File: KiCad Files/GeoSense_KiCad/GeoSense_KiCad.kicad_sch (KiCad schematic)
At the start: 127 parts, among them J0 Conn_01x04_Pin, J1 Conn_01x04_Pin, J10 Conn_01x01_Socket, J11 Conn_01x01_Socket, J12 Conn_01x01_Socket, J13 Conn_01x01_Socket, J15 Conn_01x02_Pin, J2 Conn_01x04_Pin, J3 Conn_01x04_Pin, J4 Conn_01x04_Pin, J5 Conn_01x04_Pin, J6 Conn_01x04_Pin, J7 Conn_01x04_Pin, J8 Conn_01x04_Pin, J9 Conn_01x08_Pin, U1 LM324, U1.1 LM334Z, U1.2 LM334Z, U2 LM324, U2.1 LM334Z, U2.2 LM334Z, U3 LM324, U3.1 LM334Z, U3.2 LM334Z, U4 LM324, U4.1 LM334Z, U4.2 LM334Z, U5 LM324, U5.1 LM334Z, U5.2 LM334Z, U6 LM324, U6.1 LM334Z, U6.2 LM334Z, U7 LM324, U7.1 LM334Z, U7.2 LM334Z, U8 LM324, U8.1 LM334Z, U8.2 LM334Z

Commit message: added caps
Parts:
- added C1, C10, C11, C12, C13, C14, C15, C16, C2, C3, C4, C5, C6, C7, C8, C9: C_Small, Capacitor_SMD:C_0603_1608Metric_Pad1.08x0.95mm_HandSolder, symbol Device:C_Small
- U1, U2, U3, U4, U5, U6, U7, U8: footprint (none) -> Package_SO:TSSOP-14_4.4x5mm_P0.65mm
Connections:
- net GND: now also C1.1, C10.2, C11.1, C12.2, C13.1, C14.2, C15.1, C16.2, C2.2, C3.1, C4.2, C5.1, C6.2, C7.1, C8.2, C9.1
- net T1.2 In: now also C2.1
- net T1.C: now also C1.2
- net T2.2 In: now also C4.1
- net T2.C: now also C3.2
- net T3.2 In: now also C6.1
- net T3.C: now also C5.2
- net T4.2 In: now also C8.1
- net T4.C: now also C7.2
- net T5.2 In: now also C10.1
- net T5.C: now also C9.2
- net T6.2 In: now also C12.1
- net T6.C: now also C11.2
- net T7.2 In: now also C14.1
- net T7.C: now also C13.2
- net T8.2 In: now also C16.1
- net T8.C: now also C15.2

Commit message: part way through the pcb design
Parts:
- removed J9: Conn_01x08_Pin, Connector_PinHeader_2.54mm:PinHeader_1x08_P2.54mm_Horizontal, symbol Connector:Conn_01x08_Pin
- added J14, J9: Conn_01x04_Pin, Connector_PinHeader_2.54mm:PinHeader_1x04_P2.54mm_Horizontal, symbol Connector:Conn_01x04_Pin
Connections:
- net Out 1: now also J9.1 (Pin_1)
- net Out 2: now also J9.2 (Pin_2)
- net Out 3: now also J9.3 (Pin_3)
- net Out 4: now also J9.4 (Pin_4)
- net Out 5: now also J14.1 (Pin_1)
- net Out 6: now also J14.2 (Pin_2)
- net Out 7: now also J14.3 (Pin_3)
- net Out 8: now also J14.4 (Pin_4)
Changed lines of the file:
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@@
 	)
 	(symbol
+		(lib_id "Connector:Conn_01x04_Pin")
+		(at 21.59 31.75 0)
+		(unit 1)
+		(exclude_from_sim no)
+		(in_bom yes)
+		(on_board yes)
+		(dnp no)
+		(property "Reference" "J14"
+			(at 21.844 38.354 0)
+			(effects
+				(font
+					(size 1.27 1.27)
+				)
+			)
+		)
+		(property "Value" "Conn_01x04_Pin"
+			(at 21.844 40.894 0)
+			(effects
+				(font
+					(size 1.27 1.27)
+				)
+			)
+		)
+		(property "Footprint" "Connector_PinHeader_2.54mm:PinHeader_1x04_P2.54mm_Horizontal"
+			(at 21.59 31.75 0)
+			(effects
+				(font
+					(size 1.27 1.27)
+				)
+				(hide yes)
+			)
+		)
+		(property "Datasheet" "~"
+			(at 21.59 31.75 0)
+			(effects
+				(font
+					(size 1.27 1.27)
+				)
+				(hide yes)
+			)
+		)
+		(property "Description" "Generic connector, single row, 01x04, script generated"
+			(at 21.59 31.75 0)
+			(effects
+				(font
+					(size 1.27 1.27)
+				)
+				(hide yes)
+			)
+		)
+		(pin "1"
+		)
+		(pin "3"
+		)
+		(pin "2"
+		)
+		(pin "4"
+		)
+		(instances
+			(project "GeoSense_KiCad"
+				(path "/4306debd-181b-47b9-9107-2cbe024dbb09"
+					(reference "J14")
+					(unit 1)
+				)
+			)
+		)
+	)
+	(symbol
 		(lib_id "Device:R")
 		(at 284.48 109.22 270)
@@
 	)
 	(symbol
-		(lib_id "Connector:Conn_01x08_Pin")
-		(at 21.59 26.67 0)
-		(unit 1)
-		(exclude_from_sim no)
-		(in_bom yes)
-		(on_board yes)
-		(dnp no)
-		(fields_autoplaced yes)
-		(property "Reference" "J9"
-			(at 22.225 13.97 0)
-			(effects
-				(font
-					(size 1.27 1.27)
-				)
-			)
-		)
-		(property "Value" "Conn_01x08_Pin"
-			(at 22.225 16.51 0)
-			(effects
-				(font
-					(size 1.27 1.27)
-				)
-			)
-		)
-		(property "Footprint" "Connector_PinHeader_2.54mm:PinHeader_1x08_P2.54mm_Horizontal"
-			(at 21.59 26.67 0)
-			(effects
-				(font
-					(size 1.27 1.27)
-				)
-				(hide yes)
-			)
-		)
-		(property "Datasheet" "~"
-			(at 21.59 26.67 0)
-			(effects
-				(font
-					(size 1.27 1.27)
-				)
-				(hide yes)
-			)
-		)
-		(property "Description" "Generic connector, single row, 01x08, script generated"
-			(at 21.59 26.67 0)
-			(effects
-				(font
-					(size 1.27 1.27)
-				)
-				(hide yes)
-			)
-		)
-		(pin "8"
-		)
-		(pin "6"
-		)
-		(pin "5"
-		)
-		(pin "2"
-		)
-		(pin "4"
-		)
-		(pin "7"
-		)
-		(pin "3"
-		)
-		(pin "1"
-		)
-		(instances
-			(project ""
-				(path "/4306debd-181b-47b9-9107-2cbe024dbb09"
-					(reference "J9")
-					(unit 1)
-				)
-			)
-		)
-	)
-	(symbol
 		(lib_id "Device:R")
 		(at 143.51 106.68 90)
@@
 					(unit 1)
 				)
+			)
+		)
+	)
+	(symbol
+		(lib_id "Connector:Conn_01x04_Pin")
+		(at 21.59 21.59 0)
+		(unit 1)
+		(exclude_from_sim no)
+		(in_bom yes)
+		(on_board yes)
+		(dnp no)
+		(fields_autoplaced yes)
+		(property "Reference" "J9"
+			(at 22.225 13.97 0)
+			(effects
+				(font
+					(size 1.27 1.27)
+				)
+			)
+		)
+		(property "Value" "Conn_01x04_Pin"
+			(at 22.225 16.51 0)
+			(effects
+				(font
+					(size 1.27 1.27)
+				)
+			)
+		)
+		(property "Footprint" "Connector_PinHeader_2.54mm:PinHeader_1x04_P2.54mm_Horizontal"
+			(at 21.59 21.59 0)
+			(effects
+				(font
+					(size 1.27 1.27)
+				)
+				(hide yes)
+			)
+		)
+		(property "Datasheet" "~"
+			(at 21.59 21.59 0)
+			(effects
+				(font
+					(size 1.27 1.27)
+				)
+				(hide yes)
+			)
+		)
+		(property "Description" "Generic connector, single row, 01x04, script generated"
+			(at 21.59 21.59 0)
+			(effects
+				(font
+					(size 1.27 1.27)
+				)
+				(hide yes)
+			)
+		)
+		(pin "1"
+		)
+		(pin "3"
+		)
+		(pin "2"
+		)
+		(pin "4"
+		)
+		(instances
+			(project "GeoSense_KiCad"
+				(path "/4306debd-181b-47b9-9107-2cbe024dbb09"
+					(reference "J9")
+					(unit 1)
+				)

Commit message: pcb mainly built
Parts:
- removed C10, C11, C12, C13, C14, C15, C16, C9: C_Small, Capacitor_SMD:C_0603_1608Metric_Pad1.08x0.95mm_HandSolder, symbol Device:C_Small
- C1, C2, C3, C4, C5, C6, C7, C8: footprint Capacitor_SMD:C_0603_1608Metric_Pad1.08x0.95mm_HandSolder -> Capacitor_SMD:C_0603_1608Metric
- J0, J1, J14, J2, J3, J4, J5, J6, J7, J8, J9: footprint Connector_PinHeader_2.54mm:PinHeader_1x04_P2.54mm_Horizontal -> Connector_PinHeader_2.54mm:PinHeader_1x04_P2.54mm_Vertical
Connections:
- net +5V: now also C1.2, C2.2, C3.2, C4.2, C5.2, C6.2, C7.2, C8.2
- net GND: now also C2.1, C4.1, C6.1, C8.1; no longer C2.2, C4.2, C6.2, C8.2
- net T1.2 In: no longer C2.1
- net T1.C: no longer C1.2
- net T2.2 In: no longer C4.1
- net T2.C: no longer C3.2
- net T3.2 In: no longer C6.1
- net T3.C: no longer C5.2
- net T4.2 In: no longer C8.1
- net T4.C: no longer C7.2

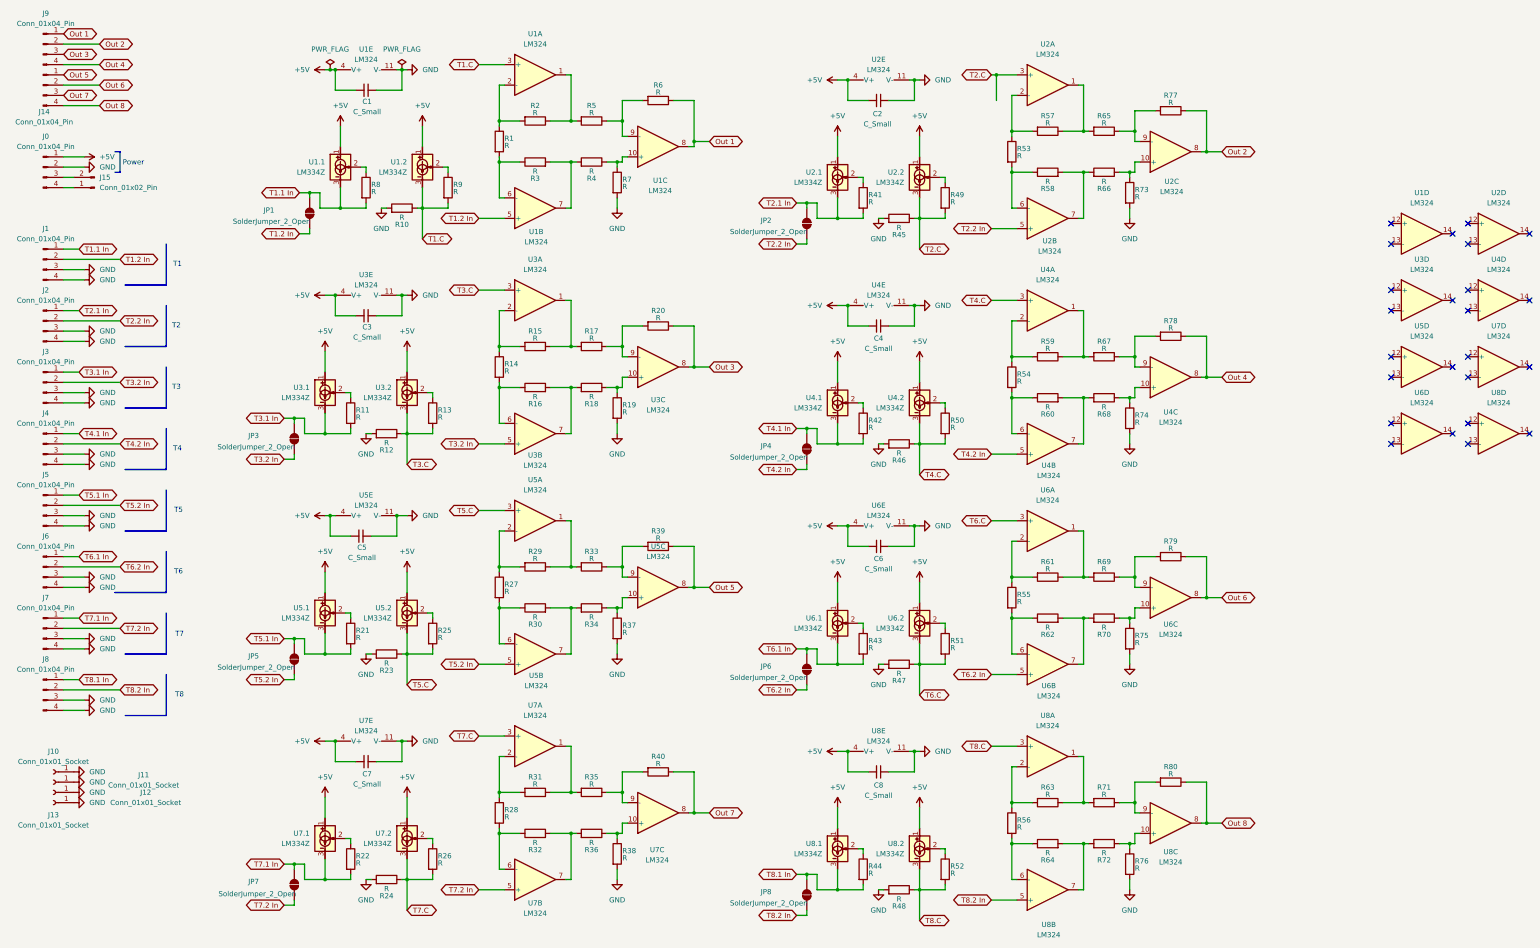
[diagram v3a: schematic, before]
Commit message: added to diodes to the schematic
need to reroute the pcb
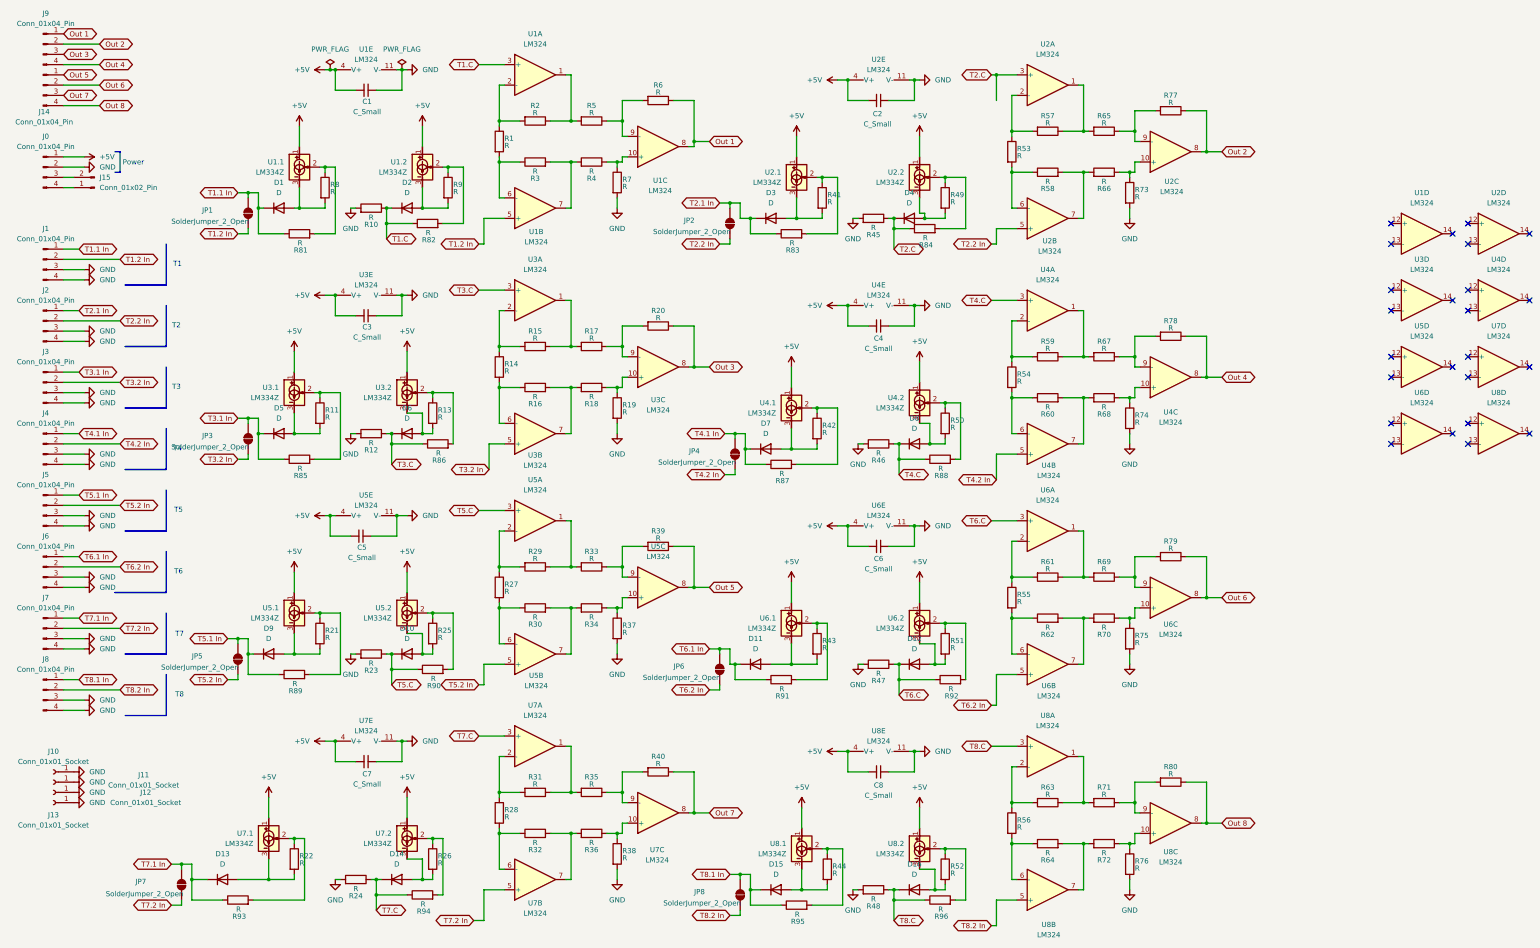
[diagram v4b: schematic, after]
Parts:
- added D1, D10, D11, D12, D13, D14, D15, D16, D2, D3, D4, D5, D6, D7, D8, D9: D, Diode_THT:D_DO-35_SOD27_P7.62mm_Horizontal, symbol Device:D
- added R81, R82, R83, R84, R85, R86, R87, R88, R89, R90, R91, R92, R93, R94, R95, R96: R, Resistor_THT:R_Axial_DIN0204_L3.6mm_D1.6mm_P5.08mm_Horizontal, symbol Device:R
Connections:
- net T1.1 In: now also D1.1 (K), R81.1; no longer R8.2, U1.1.3
- net T1.C: now also D2.1 (K), R82.1; no longer R9.2, U1.2.3
- net T2.1 In: now also D3.1 (K), R83.1; no longer R41.2, U2.1.3
- net T2.C: now also D4.1 (K), R84.1; no longer R49.2, U2.2.3
- net T3.1 In: now also D5.1 (K), R85.1; no longer R11.2, U3.1.3
- net T3.C: now also D6.1 (K), R86.1; no longer R13.2, U3.2.3
- net T4.1 In: now also D7.1 (K), R87.1; no longer R42.2, U4.1.3
- net T4.C: now also D8.1 (K), R88.1; no longer R50.2, U4.2.3
- net T5.1 In: now also D9.1 (K), R89.1; no longer R21.2, U5.1.3
- net T5.C: now also D10.1 (K), R90.1; no longer R25.2, U5.2.3
- net T6.1 In: now also D11.1 (K), R91.1; no longer R43.2, U6.1.3
- net T6.C: now also D12.1 (K), R92.1; no longer R51.2, U6.2.3
- net T7.1 In: now also D13.1 (K), R93.1; no longer R22.2, U7.1.3
- net T7.C: now also D14.1 (K), R94.1; no longer R26.2, U7.2.3
- net T8.1 In: now also D15.1 (K), R95.1; no longer R44.2, U8.1.3
- net T8.C: now also D16.1 (K), R96.1; no longer R52.2, U8.2.3
- net at R41.1, U2.1.2: now also R83.2
- net at R9.1, U1.2.2: now also R82.2
- net at R8.1, U1.1.2: now also R81.2
- net at R50.1, U4.2.2: now also R88.2
- net at R44.1, U8.1.2: now also R95.2
- net at R51.1, U6.2.2: now also R92.2
- net at R42.1, U4.1.2: now also R87.2
- net at R25.1, U5.2.2: now also R90.2
- net at R21.1, U5.1.2: now also R89.2
- net at R26.1, U7.2.2: now also R94.2
- net at R13.1, U3.2.2: now also R86.2
- net at R52.1, U8.2.2: now also R96.2
- net at R43.1, U6.1.2: now also R91.2
- net at R49.1, U2.2.2: now also R84.2
- net at R22.1, U7.1.2: now also R93.2
- net at R11.1, U3.1.2: now also R85.2
- new net: D7.2 (A), R42.2, U4.1.3
- new net: D3.2 (A), R41.2, U2.1.3
- new net: D2.2 (A), R9.2, U1.2.3
- new net: D1.2 (A), R8.2, U1.1.3
- new net: D8.2 (A), R50.2, U4.2.3
- new net: D15.2 (A), R44.2, U8.1.3
- new net: D11.2 (A), R43.2, U6.1.3
- new net: D12.2 (A), R51.2, U6.2.3
- new net: D10.2 (A), R25.2, U5.2.3
- new net: D13.2 (A), R22.2, U7.1.3
- new net: D9.2 (A), R21.2, U5.1.3
- new net: D14.2 (A), R26.2, U7.2.3
- new net: D6.2 (A), R13.2, U3.2.3
- new net: D16.2 (A), R52.2, U8.2.3
- new net: D4.2 (A), R49.2, U2.2.3
- new net: D5.2 (A), R11.2, U3.1.3
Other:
- moved on the sheet: JP1, JP2, JP3, JP4, JP5, JP6, JP7, JP8, R10, R11, R12, R21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

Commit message: updated to kicad 9.0.1
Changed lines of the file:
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@@
 (kicad_sch
-	(version 20231120)
+	(version 20250114)
 	(generator "eeschema")
-	(generator_version "8.0")
+	(generator_version "9.0")
 	(paper "A3")
 	(title_block
@@
 		(rev "1")
 	)
+	(text "T3\n"
+		(exclude_from_sim no)
+		(at 54.61 106.68 0)
+		(effects
+			(font
+				(size 1.27 1.27)
+			)
+		)
+	)
+	(text "T1"
+		(exclude_from_sim no)
+		(at 54.864 76.2 0)
+		(effects
+			(font
+				(size 1.27 1.27)
+			)
+		)
+	)
+	(text "T2\n"
+		(exclude_from_sim no)
+		(at 54.61 91.44 0)
+		(effects
+			(font
+				(size 1.27 1.27)
+			)
+		)
+	)
+	(text "Power"
+		(exclude_from_sim no)
+		(at 43.942 51.054 0)
+		(effects
+			(font
+				(size 1.27 1.27)
+			)
+		)
+	)
+	(text "T7"
+		(exclude_from_sim no)
+		(at 55.372 167.894 0)
+		(effects
+			(font
+				(size 1.27 1.27)
+			)
+		)
+	)
+	(text "T5"
+		(exclude_from_sim no)
+		(at 55.118 137.16 0)
+		(effects
+			(font
+				(size 1.27 1.27)
+			)
+		)
+	)
+	(text "T6"
+		(exclude_from_sim no)
+		(at 55.118 152.4 0)
+		(effects
+			(font
+				(size 1.27 1.27)
+			)
+		)
+	)
+	(text "T8"
+		(exclude_from_sim no)
+		(at 55.372 182.88 0)
+		(effects
+			(font
+				(size 1.27 1.27)
+			)
+		)
+	)
+	(text "T4"
+		(exclude_from_sim no)
+		(at 54.864 121.92 0)
+		(effects
+			(font
+				(size 1.27 1.27)
+			)
+		)
+	)
 	(junction
 		(at 90.17 107.95)
@@
 	)
 	(junction
-		(at 257.81 29.21)
-		(diameter 0)
-		(color 0 0 0 0)
-	)
-	(junction
 		(at 245.11 110.49)
 		(diameter 0)
@@
 	(wire
 		(pts
-			(xy 257.81 29.21) (xy 262.89 29.21)
+			(xy 256.54 29.21) (xy 262.89 29.21)
 		)
 		(stroke
@@
 	(wire
 		(pts
-			(xy 257.81 29.21) (xy 257.81 35.56)
-		)
-		(stroke
-			(width 0)
-			(type default)
-		)
-	)
-	(wire
-		(pts
 			(xy 88.9 68.58) (xy 93.98 68.58)
 		)
@@
 	(wire
 		(pts
-			(xy 256.54 29.21) (xy 257.81 29.21)
-		)
-		(stroke
-			(width 0)
-			(type default)
-		)
-	)
-	(wire
-		(pts
 			(xy 165.1 44.45) (xy 166.37 44.45)
 		)
@@
 		)
 	)
-	(text "T3\n"
-		(exclude_from_sim no)
-		(at 54.61 106.68 0)
-		(effects
-			(font
-				(size 1.27 1.27)
-			)
-		)
-	)
-	(text "T1"
-		(exclude_from_sim no)
-		(at 54.864 76.2 0)
-		(effects
-			(font
-				(size 1.27 1.27)
-			)
-		)
-	)
-	(text "T2\n"
-		(exclude_from_sim no)
-		(at 54.61 91.44 0)
-		(effects
-			(font
-				(size 1.27 1.27)
-			)
-		)
-	)
-	(text "Power"
-		(exclude_from_sim no)
-		(at 43.942 51.054 0)
-		(effects
-			(font
-				(size 1.27 1.27)
-			)
-		)
-	)
-	(text "T7"
-		(exclude_from_sim no)
-		(at 55.372 167.894 0)
-		(effects
-			(font
-				(size 1.27 1.27)
-			)
-		)
-	)
-	(text "T5"
-		(exclude_from_sim no)
-		(at 55.118 137.16 0)
-		(effects
-			(font
-				(size 1.27 1.27)
-			)
-		)
-	)
-	(text "T6"
-		(exclude_from_sim no)
-		(at 55.118 152.4 0)
-		(effects
-			(font
-				(size 1.27 1.27)
-			)
-		)
-	)
-	(text "T8"
-		(exclude_from_sim no)
-		(at 55.372 182.88 0)
-		(effects
-			(font
-				(size 1.27 1.27)
-			)
-		)
-	)
-	(text "T4"
-		(exclude_from_sim no)
-		(at 54.864 121.92 0)
-		(effects
-			(font
-				(size 1.27 1.27)
-			)
-		)
-	)
 	(global_label "T4.2 In"
 		(shape bidirectional)
@@
 	)
 	(symbol
+		(lib_id "GeoSenseGFnLogo:LOGO")
+		(at 359.41 31.75 0)
+		(unit 1)
+		(exclude_from_sim no)
+		(in_bom yes)
+		(on_board yes)
+		(dnp no)
+		(fields_autoplaced yes)
+		(property "Reference" "#G1"
+			(at 359.41 19.1347 0)
+			(effects
+				(font
+					(size 1.27 1.27)
+				)
+				(hide yes)
+			)
+		)
+		(property "Value" "LOGO"
+			(at 359.41 44.3653 0)
+			(effects
+				(font
+					(size 1.27 1.27)
+				)
+				(hide yes)
+			)
+		)
+		(property "Footprint" "Logo kicad:GeoSenseGFnLogo"
+			(at 359.41 31.75 0)
+			(effects
+				(font
+					(size 1.27 1.27)
+				)
+				(hide yes)
+			)
+		)
+		(property "Datasheet" ""
+			(at 359.41 31.75 0)
+			(effects
+				(font
+					(size 1.27 1.27)
+				)
+				(hide yes)
+			)
+		)
+		(property "Description" ""
+			(at 359.41 31.75 0)
+			(effects
+				(font
+					(size 1.27 1.27)
+				)
+				(hide yes)
+			)
+		)
+		(instances
+			(project ""
+				(path "/4306debd-181b-47b9-9107-2cbe024dbb09"
+					(reference "#G1")
+					(unit 1)
+				)
+			)
+		)
+	)
+	(symbol
 		(lib_id "Device:R")
 		(at 290.83 224.79 0)
@@
 		)
 	)
+	(embedded_fonts no)
 )
